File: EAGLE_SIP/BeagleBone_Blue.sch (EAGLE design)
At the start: 215 parts, among them IC1 WL1835MODGBMOCT, J1 USD_CONNECTOR, M1 JST_ZH_2, M2 JST_ZH_2, M3 JST_ZH_2, M4 JST_ZH_2, Q3 MOSFET-N, U1 LOGIC-TXS0102DCTR(MSOP8), U5 24LC_32AT-I/OT, U6 SN74LVC1G07_DCK_5, U8 MTFC4GLDEA, Y1 CM200C-32.768KAZF-UT, Y2 445C33D24M00000

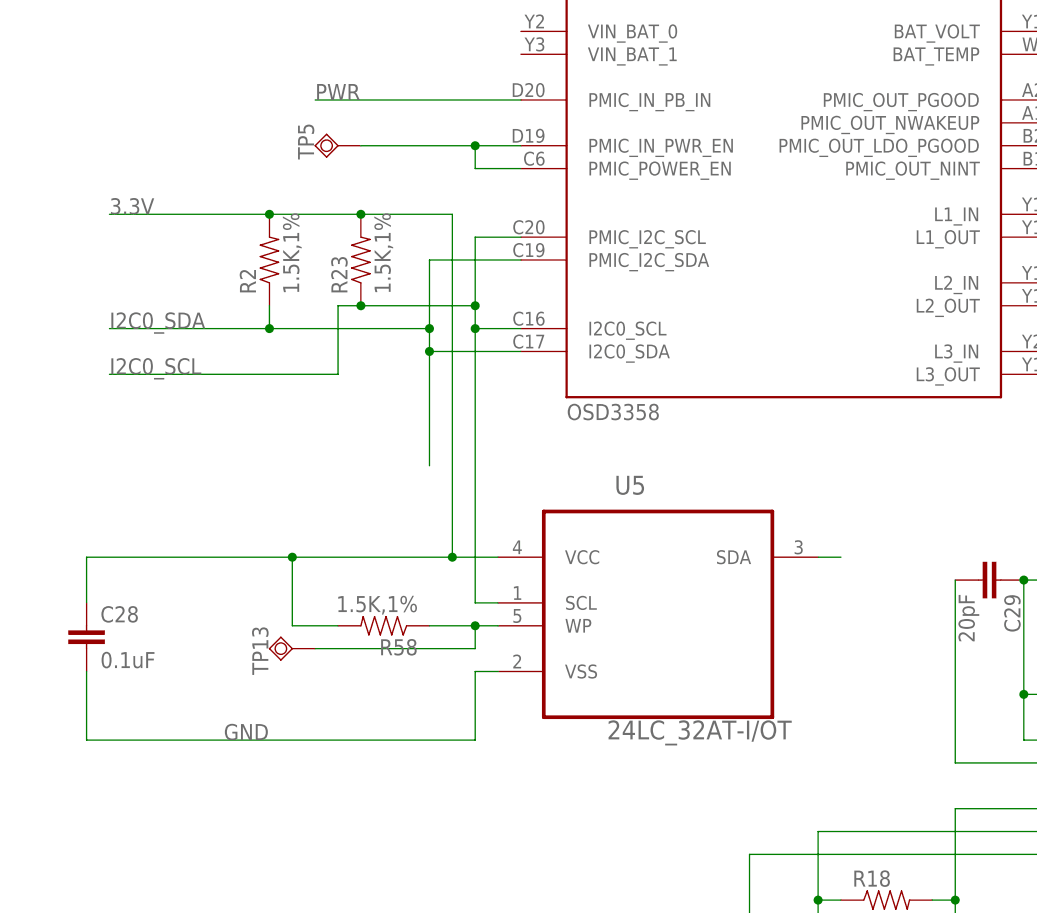
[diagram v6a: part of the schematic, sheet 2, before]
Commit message: Fixed I2C EEPROM wiring.
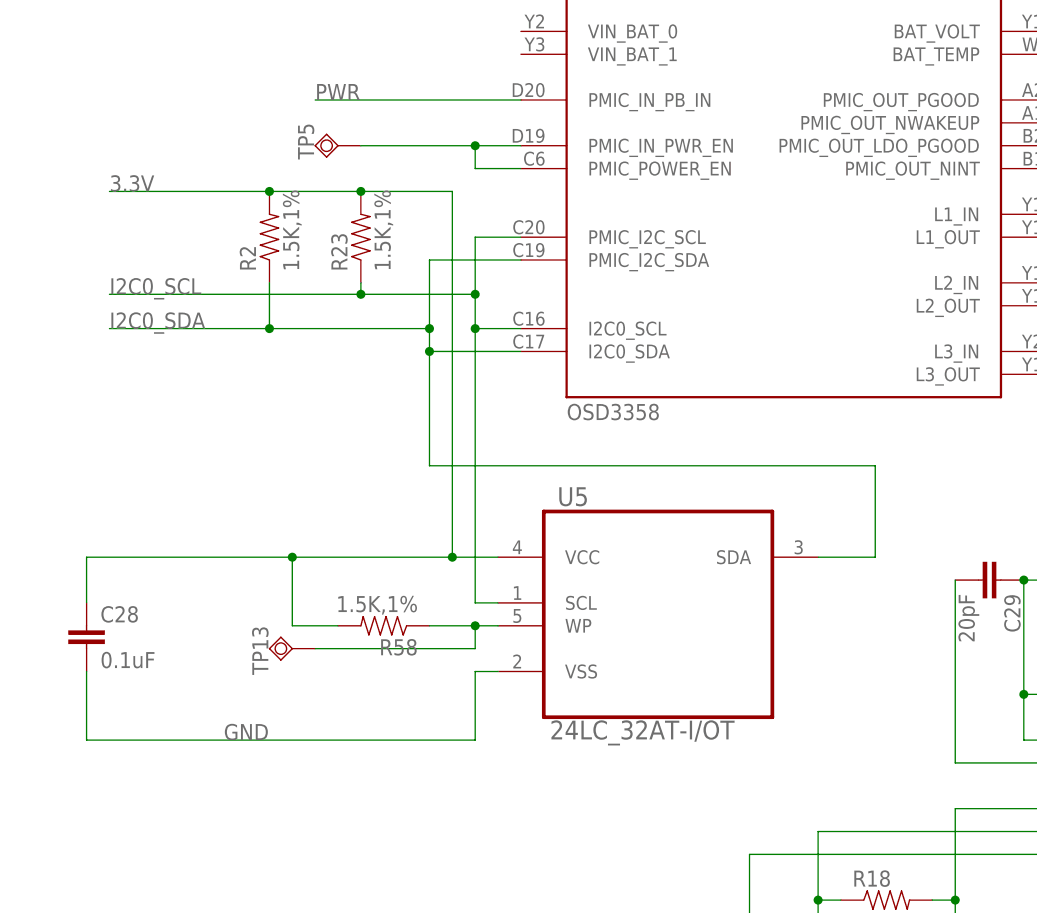
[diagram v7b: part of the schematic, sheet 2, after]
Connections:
- removed net N$86: U5.SDA
- net I2C0_SDA: now also U5.SDA
- net UART1_RX: no longer CAN.3
- net UART1_TX: no longer CAN.4
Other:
- moved on the sheet: R2, R23
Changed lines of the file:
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@@
 <label x="161.29" y="35.56" size="1.778" layer="95"/>
-</segment>
-<segment>
-<pinref part="CAN" gate="G$1" pin="4"/>
-<wire x1="172.72" y1="10.16" x2="160.02" y2="10.16" width="0.1524" layer="91"/>
-<label x="161.29" y="10.16" size="1.778" layer="95"/>
 </segment>
 </net>
@@
 <wire x1="172.72" y1="38.1" x2="160.02" y2="38.1" width="0.1524" layer="91"/>
 <label x="161.29" y="38.1" size="1.778" layer="95"/>
-</segment>
-<segment>
-<pinref part="CAN" gate="G$1" pin="3"/>
-<wire x1="172.72" y1="12.7" x2="160.02" y2="12.7" width="0.1524" layer="91"/>
-<label x="161.29" y="12.7" size="1.778" layer="95"/>
 </segment>
 </net>
@@
 <instance part="TP1" gate="G$1" x="137.16" y="243.84" rot="R90"/>
 <instance part="TP5" gate="G$1" x="45.72" y="210.82" rot="R270"/>
-<instance part="R2" gate="G$1" x="38.1" y="198.12" rot="R90"/>
-<instance part="R23" gate="G$1" x="48.26" y="198.12" rot="R90"/>
+<instance part="R2" gate="G$1" x="38.1" y="200.66" rot="R90"/>
+<instance part="R23" gate="G$1" x="48.26" y="200.66" rot="R90"/>
 <instance part="D8" gate="G$1" x="160.02" y="233.68" rot="R90"/>
 <instance part="R24" gate="G$1" x="193.04" y="233.68"/>
@@
 <attribute name="VALUE" x="124.46" y="157.48" size="1.778" layer="96"/>
 </instance>
-<instance part="U5" gate="A" x="63.5" y="165.1"/>
+<instance part="U5" gate="A" x="63.5" y="165.1" smashed="yes">
+<attribute name="NAME" x="70.0786" y="170.7896" size="2.0828" layer="95" ratio="10" rot="SR0"/>
+<attribute name="VALUE" x="69.2404" y="144.8562" size="2.0828" layer="96" ratio="10" rot="SR0"/>
+</instance>
 <instance part="R58" gate="G$1" x="50.8" y="157.48" rot="R180"/>
 <instance part="TP13" gate="G$1" x="40.64" y="154.94" rot="R270"/>
@@
 <pinref part="SIP" gate="A" pin="I2C0_SCL"/>
 <wire x1="66.04" y1="190.5" x2="60.96" y2="190.5" width="0.1524" layer="91"/>
-<wire x1="60.96" y1="190.5" x2="60.96" y2="193.04" width="0.1524" layer="91"/>
 <pinref part="SIP" gate="A" pin="PMIC_I2C_SCL"/>
-<wire x1="60.96" y1="193.04" x2="60.96" y2="200.66" width="0.1524" layer="91"/>
+<wire x1="60.96" y1="190.5" x2="60.96" y2="194.31" width="0.1524" layer="91"/>
+<wire x1="60.96" y1="194.31" x2="60.96" y2="200.66" width="0.1524" layer="91"/>
 <wire x1="60.96" y1="200.66" x2="66.04" y2="200.66" width="0.1524" layer="91"/>
-<pinref part="R23" gate="G$1" pin="1"/>
-<wire x1="48.26" y1="193.04" x2="60.96" y2="193.04" width="0.1524" layer="91"/>
-<junction x="60.96" y="193.04"/>
-<wire x1="48.26" y1="193.04" x2="45.72" y2="193.04" width="0.1524" layer="91"/>
-<wire x1="45.72" y1="193.04" x2="45.72" y2="185.42" width="0.1524" layer="91"/>
-<junction x="48.26" y="193.04"/>
-<wire x1="45.72" y1="185.42" x2="20.32" y2="185.42" width="0.1524" layer="91"/>
-<label x="20.32" y="185.42" size="1.778" layer="95"/>
 <wire x1="60.96" y1="190.5" x2="60.96" y2="160.02" width="0.1524" layer="91"/>
 <junction x="60.96" y="190.5"/>
 <wire x1="60.96" y1="160.02" x2="63.5" y2="160.02" width="0.1524" layer="91"/>
 <pinref part="U5" gate="A" pin="SCL"/>
+<wire x1="60.96" y1="194.31" x2="48.26" y2="194.31" width="0.1524" layer="91"/>
+<label x="20.32" y="194.31" size="1.778" layer="95"/>
+<junction x="60.96" y="194.31"/>
+<junction x="48.26" y="194.31"/>
+<wire x1="48.26" y1="194.31" x2="20.32" y2="194.31" width="0.1524" layer="91"/>
+<pinref part="R23" gate="G$1" pin="1"/>
+<wire x1="48.26" y1="195.58" x2="48.26" y2="194.31" width="0.1524" layer="91"/>
 </segment>
 </net>
@@
 <wire x1="55.88" y1="187.96" x2="66.04" y2="187.96" width="0.1524" layer="91"/>
 <pinref part="R2" gate="G$1" pin="1"/>
-<wire x1="38.1" y1="193.04" x2="38.1" y2="190.5" width="0.1524" layer="91"/>
+<wire x1="38.1" y1="195.58" x2="38.1" y2="190.5" width="0.1524" layer="91"/>
 <wire x1="38.1" y1="190.5" x2="55.88" y2="190.5" width="0.1524" layer="91"/>
 <junction x="55.88" y="190.5"/>
@@
 <wire x1="55.88" y1="187.96" x2="55.88" y2="175.26" width="0.1524" layer="91"/>
 <junction x="55.88" y="187.96"/>
+<wire x1="55.88" y1="175.26" x2="105.41" y2="175.26" width="0.1524" layer="91"/>
+<wire x1="105.41" y1="175.26" x2="105.41" y2="165.1" width="0.1524" layer="91"/>
+<pinref part="U5" gate="A" pin="SDA"/>
+<wire x1="105.41" y1="165.1" x2="99.06" y2="165.1" width="0.1524" layer="91"/>
 </segment>
 </net>
@@
 <wire x1="40.64" y1="165.1" x2="17.78" y2="165.1" width="0.1524" layer="91"/>
 <wire x1="17.78" y1="165.1" x2="17.78" y2="160.02" width="0.1524" layer="91"/>
-<wire x1="58.42" y1="165.1" x2="58.42" y2="203.2" width="0.1524" layer="91"/>
+<wire x1="58.42" y1="165.1" x2="58.42" y2="205.74" width="0.1524" layer="91"/>
 <junction x="58.42" y="165.1"/>
 <pinref part="R23" gate="G$1" pin="2"/>
-<wire x1="58.42" y1="203.2" x2="48.26" y2="203.2" width="0.1524" layer="91"/>
+<wire x1="58.42" y1="205.74" x2="48.26" y2="205.74" width="0.1524" layer="91"/>
 <pinref part="R2" gate="G$1" pin="2"/>
-<wire x1="38.1" y1="203.2" x2="48.26" y2="203.2" width="0.1524" layer="91"/>
-<junction x="48.26" y="203.2"/>
-<wire x1="38.1" y1="203.2" x2="20.32" y2="203.2" width="0.1524" layer="91"/>
-<junction x="38.1" y="203.2"/>
-<label x="20.32" y="203.2" size="1.778" layer="95"/>
+<wire x1="38.1" y1="205.74" x2="48.26" y2="205.74" width="0.1524" layer="91"/>
+<junction x="48.26" y="205.74"/>
+<wire x1="38.1" y1="205.74" x2="20.32" y2="205.74" width="0.1524" layer="91"/>
+<junction x="38.1" y="205.74"/>
+<label x="20.32" y="205.74" size="1.778" layer="95"/>
 <wire x1="40.64" y1="157.48" x2="40.64" y2="165.1" width="0.1524" layer="91"/>
 <junction x="40.64" y="165.1"/>
@@
 </segment>
 </net>
-<net name="N$86" class="0">
-<segment>
-<wire x1="101.6" y1="165.1" x2="99.06" y2="165.1" width="0.1524" layer="91"/>
-<pinref part="U5" gate="A" pin="SDA"/>
-</segment>
-</net>

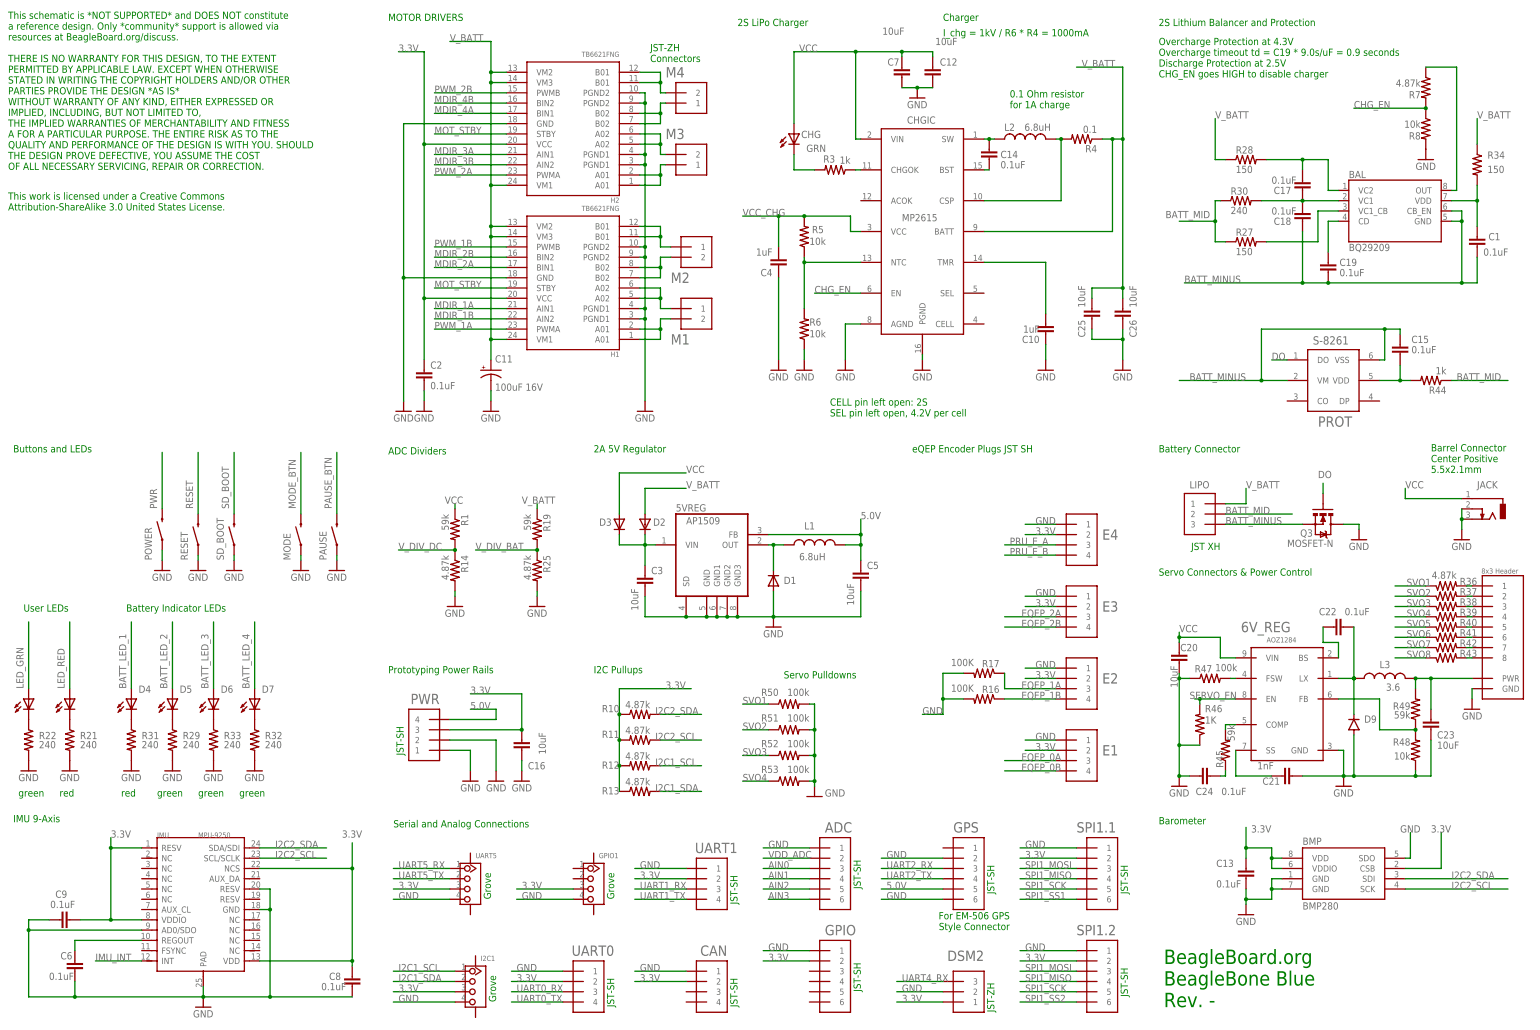
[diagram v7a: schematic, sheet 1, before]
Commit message: Wired MMC0 pull ups.  Moved components on page 1.
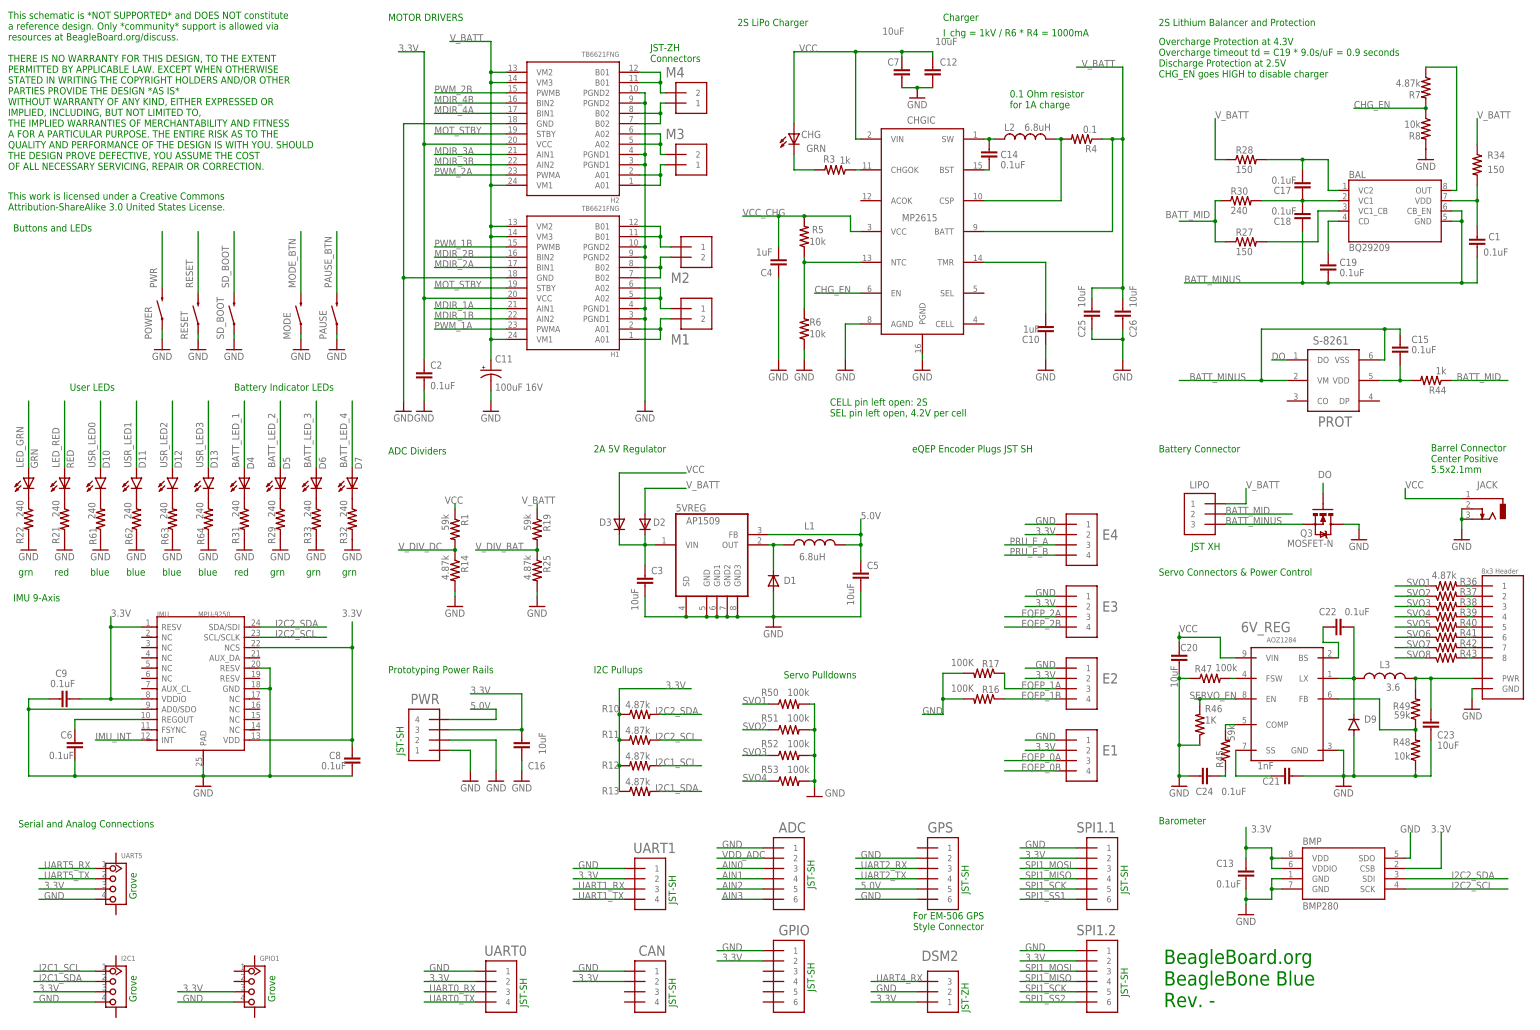
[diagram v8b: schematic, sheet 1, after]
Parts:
- added R26, R35, R54, R55, R56, R57, R65: 10K,1%, Strawson_Eagle_Lib:RESISTOR0402-RES
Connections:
- net N$43 renamed USR_LED3
- net N$44 renamed USR_LED2
- net N$45 renamed USR_LED1
- net N$46 renamed USR_LED0
- net PWR_LEDR renamed PWR_LED
- new net N$86: J1.VCC
- net N$2: now also R57.1
- net N$5: now also R26.1
- net N$70: now also R54.1
- net N$74: now also R56.1
- net N$75: now also R65.1
- net N$77: now also R55.1
- net NTE: now also R35.1
- net VCC_3V3B: now also R54.2, R55.2, R56.2, R57.2, R65.2; no longer C35.2, J1.VCC
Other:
- note added: "blue"
- note added: "grn"
- note removed: "green"
- moved on the sheet: ADC, C31, C32, C34, C35, C6, C8, C9, CAN, D4, D5, D6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
